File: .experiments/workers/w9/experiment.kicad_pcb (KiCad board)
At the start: 2 copper layers, 140 x 90 mm, 39 parts, among them J1 USB_C, J2 Output, J3 Debug, Q1 FS8205A, U1 USBLC6-2SC6, U2 BQ24072, U3 HY2113-KB5B, U4 MT3608, U5 AP2112K-3.3, U6 LN61CN3302MR-G

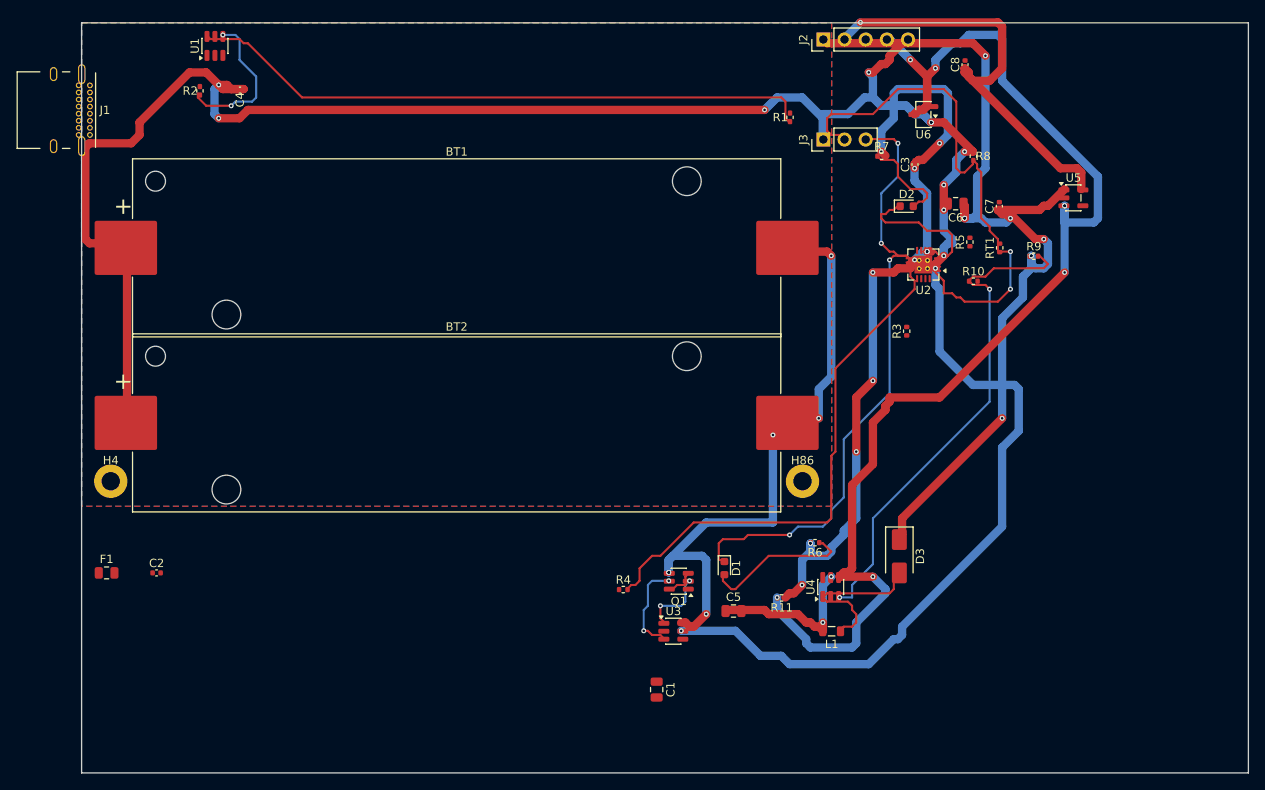
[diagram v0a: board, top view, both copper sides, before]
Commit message: 35-round experiment: best score 25.33, improved routing params
Router and conflict resolution tuning from autonomous optimization loop.
Best config: clearance=0.2051mm, cooling_factor=0.9735, existing_trace_cost=200.0

Co-Authored-By: Claude Opus 4.6 <noreply@anthropic.com>
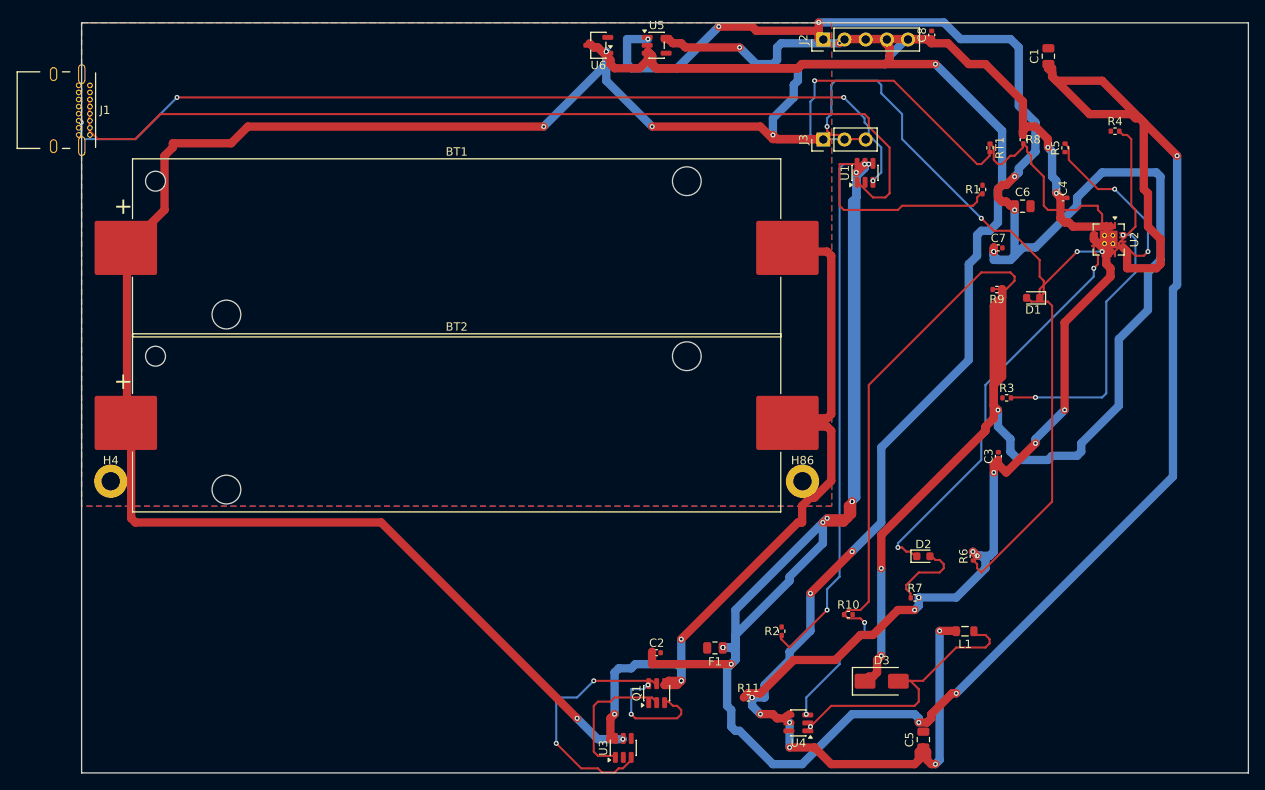
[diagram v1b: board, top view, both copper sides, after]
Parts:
- moved C4 99.6 mm to (117.8, 21.0), turned to 0 degrees
- moved R2 95.3 mm to (84.0, 73.0)
- moved C1 89.4 mm to (116.0, 4.00), turned to 90 degrees
- moved R4 80.7 mm to (124.0, 13.0)
- moved U1 79.5 mm to (94.0, 18.0)
- moved F1 73.6 mm to (76.0, 75.0), turned to 180 degrees
- moved C2 60.8 mm to (69.0, 75.6)
- moved U5 53.2 mm to (69.0, 2.69)
- moved R7 53.2 mm to (100.0, 69.0)
- moved D1 49.2 mm to (114.2, 33.0), turned to 180 degrees
- moved R10 42.7 mm to (92.0, 71.0)
- moved D2 42.0 mm to (101.0, 64.0)
- moved U6 39.9 mm to (62.0, 2.69)
- moved C3 36.4 mm to (110.0, 52.0)
- moved C5 27.5 mm to (101.0, 86.0), turned to 90 degrees
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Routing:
- net /VBUS: track 0.00 -> 327.5 mm, vias 0 -> 12
- net /5V: track 115.5 -> 241.0 mm, vias 8 -> 10
- net Net-(J1-CC1): track 0.00 -> 114.4 mm
- net Net-(J1-CC2): track 0.00 -> 107.8 mm, vias 0 -> 4
- net Net-(R1-Pad1): track 75.5 -> 25.3 mm
- net Net-(R2-Pad1): track 18.4 -> 66.1 mm
- net Net-(U2-ILIM): track 62.7 -> 16.7 mm
- net Net-(U2-ISET): track 0.00 -> 33.4 mm, vias 0 -> 2
- net Net-(D2-K): track 18.7 -> 49.6 mm, vias 0 -> 2
- net /EN: track 149.0 -> 179.1 mm, vias 8 -> 6
- net Net-(D1-A): track 17.7 -> 40.8 mm
- net /VSYS_BOOST: track 19.4 -> 42.4 mm, vias 2 -> 4
- net /CELL_NEG: track 75.5 -> 98.0 mm, vias 6 -> 5
- net Net-(U2-TMR): track 0.00 -> 22.1 mm, vias 0 -> 2
- net Net-(Q1B-G): track 11.3 -> 29.8 mm
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
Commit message: 45-round experiment: best score 25.66, all nets routed (26/26)
Fixed A* performance by increasing max_search from 100k->500k to handle
high trace costs (100.0) without timing out. Kept high cost + coarse grid
(0.5mm) to prevent shorts while still routing efficiently.

Best config: edge_margin=5.7493mm, cooling_factor=0.9764, existing_trace_cost=200, max_rips=8

Co-Authored-By: Claude Opus 4.6 <noreply@anthropic.com>
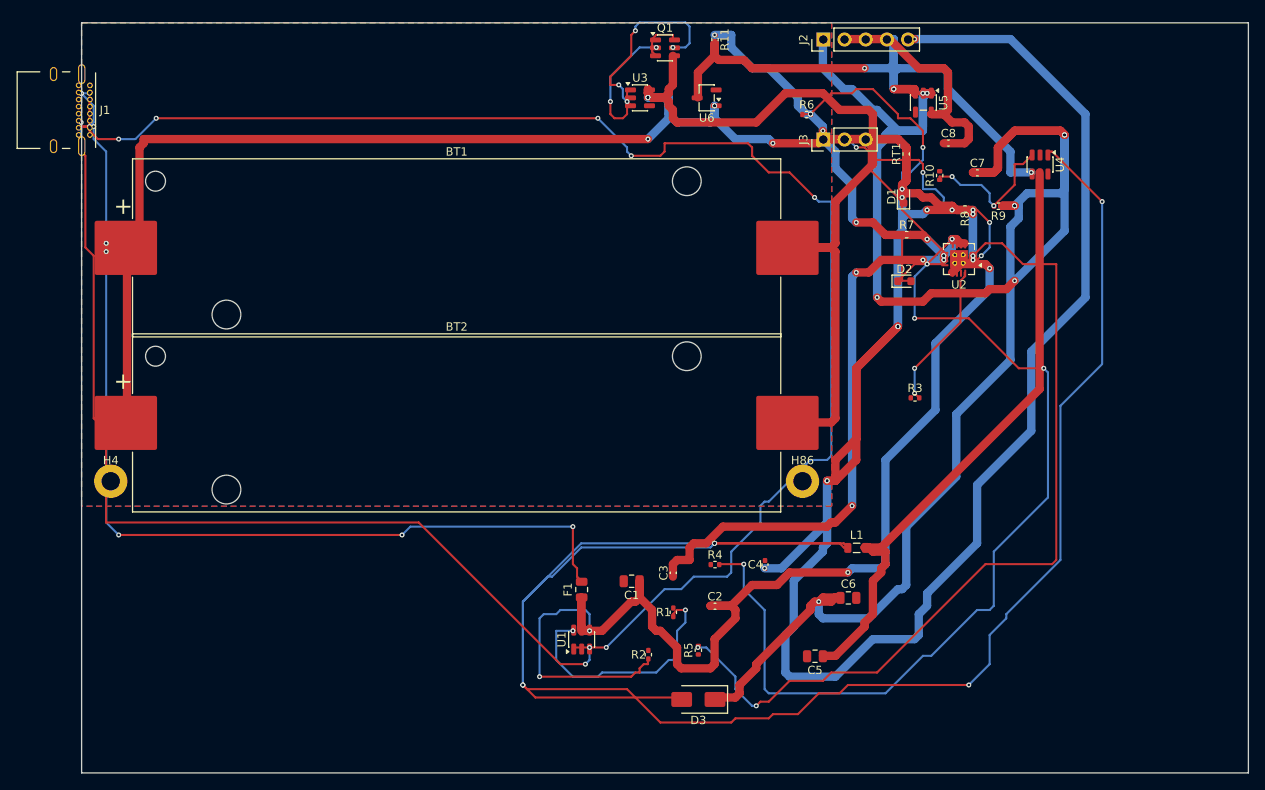
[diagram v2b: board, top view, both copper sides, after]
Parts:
- moved C1 80.4 mm to (66.0, 67.0), turned to 180 degrees
- moved R11 79.1 mm to (76.0, 2.00), turned to -90 degrees
- moved U3 78.0 mm to (67.0, 9.00), turned to 0 degrees
- moved Q1 77.4 mm to (70.0, 3.00), turned to 0 degrees
- moved R5 74.6 mm to (74.0, 75.3)
- moved U4 73.0 mm to (115.0, 17.0), turned to -90 degrees
- moved R4 70.8 mm to (76.0, 65.0)
- moved U1 65.5 mm to (60.0, 74.0)
- moved R1 62.8 mm to (71.0, 70.7)
- moved C4 56.7 mm to (82.0, 65.0), turned to 90 degrees
- moved R6 56.6 mm to (87.0, 11.0), turned to 0 degrees
- moved R10 53.8 mm to (103.0, 18.3), turned to 90 degrees
- moved C6 51.4 mm to (92.0, 69.0)
- moved R7 43.6 mm to (99.0, 25.4)
- moved C3 41.4 mm to (71.0, 66.0)
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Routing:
- net Net-(D3-A): track 35.1 -> 255.2 mm, vias 0 -> 6
- net /VBUS: track 327.5 -> 115.0 mm, vias 12 -> 2
- net /VBAT: track 279.5 -> 422.6 mm, vias 10 -> 18
- net Net-(F1-Pad2): track 0.00 -> 120.4 mm, vias 0 -> 10
- net /EN: track 179.1 -> 74.1 mm
- net Net-(U2-ILIM): track 16.7 -> 109.6 mm, vias 0 -> 4
- net Net-(U2-TMR): track 22.1 -> 104.0 mm
- net Net-(J1-CC1): track 114.4 -> 175.0 mm, vias 0 -> 6
- net Net-(U4-FB): track 73.1 -> 17.5 mm
- net /CHG_N: track 62.4 -> 17.4 mm, vias 4 -> 0
- net Net-(D2-K): track 49.6 -> 8.86 mm, vias 2 -> 0
- net Net-(R2-Pad1): track 66.1 -> 30.0 mm
- net /NTC_SENSE: track 64.9 -> 30.1 mm, vias 2 -> 6
- net /VSYS_BOOST: track 42.4 -> 74.1 mm, vias 4 -> 0
- net /VSYS: track 90.0 -> 115.1 mm, vias 8 -> 14
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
